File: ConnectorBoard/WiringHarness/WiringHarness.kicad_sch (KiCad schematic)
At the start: 36 parts, among them J1 Barrel_Jack, J3 Conn_ARM_SWD_TagConnect_TC203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, J4 Conn_02x05_Odd_Even, J5 Socket, J6 Qwiic, J7 Conn_02x12_Odd_Even, U1 PCA9306DCTR, U3 LDL212PV33R, U6 STM32C031G4Ux, U7 LDL212PU50R, U8 LD1085D2MTR

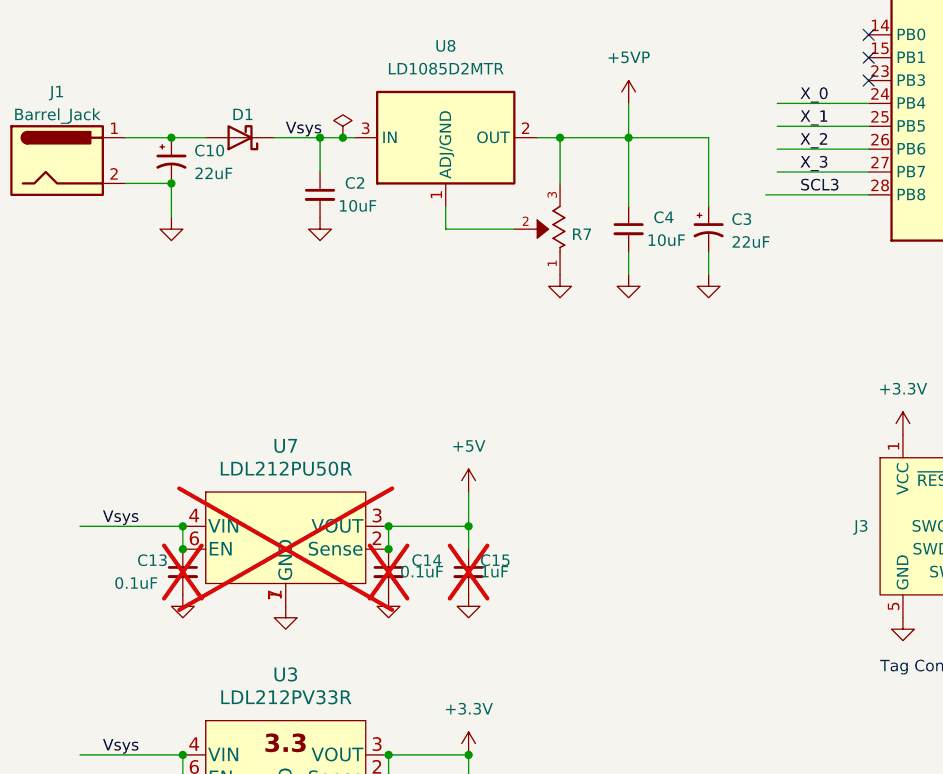
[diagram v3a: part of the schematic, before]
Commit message: switch to step models for many components
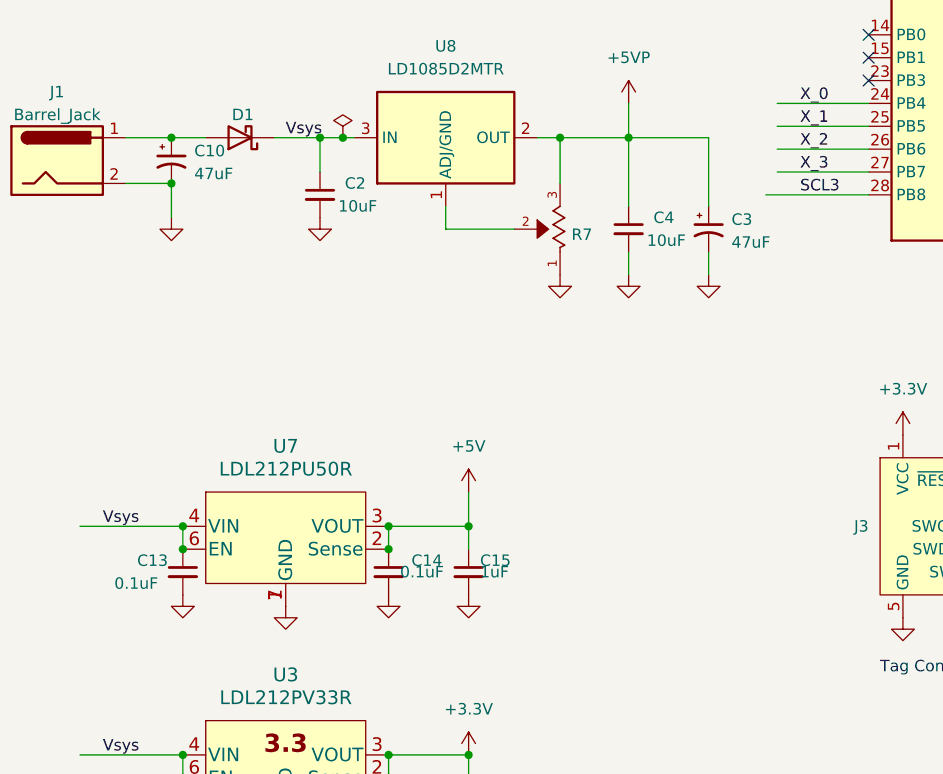
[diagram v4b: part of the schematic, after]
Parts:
- C10, C3: value 22uF -> 47uF; Digikey P16405CT-ND -> 10-ECE-A1EKA470ICT-ND; Vendor P16405CT-ND -> 10-ECE-A1EKA470ICT-ND
- C13, C14, C15, U7: now fitted
- C6: Vendor (none) -> CL10B105KA8NFNC; now left out of the parts list
- FB1: Vendor (none) -> 490-16660-1-ND; now left out of the parts list
- J6, U1: now left out of the parts list
- R1, R2: Digikey RMCF0603FT10K0DKR-ND -> RMCF0603FT10K0CT-ND; Vendor RMCF0603FT10K0DKR-ND -> RMCF0603FT10K0CT-ND; now left out of the parts list
- R7: Digikey TC33X-102ECT-ND -> TC33X-103ECT-ND; Vendor TC33X-102ECT-ND -> TC33X-103ECT-ND
- U6: Digikey 497-STM32C031G4U6-ND -> 497-STM32C031G6U6-ND; Vendor 497-STM32C031G4U6-ND -> 497-STM32C031G6U6-ND
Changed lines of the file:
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@@
       (effects (font (size 1.27 1.27)) hide)
     )
-    (property "Digikey" "497-STM32C031G4U6-ND" (at 129.54 52.07 0)
-      (effects (font (size 1.27 1.27)) hide)
-    )
-    (property "Vendor" "497-STM32C031G4U6-ND" (at 129.54 52.07 0)
+    (property "Digikey" "497-STM32C031G6U6-ND" (at 129.54 52.07 0)
+      (effects (font (size 1.27 1.27)) hide)
+    )
+    (property "Vendor" "497-STM32C031G6U6-ND" (at 129.54 52.07 0)
       (effects (font (size 1.27 1.27)) hide)
     )
@@
   )
   (symbol (lib_id "StockedComponents:C_1U") (at 198.12 60.96 0) (unit 1)
-    (in_bom yes) (on_board yes) (dnp yes) (fields_autoplaced)
+    (in_bom no) (on_board yes) (dnp yes) (fields_autoplaced)
     (property "Reference" "C6" (at 200.66 59.6963 0)
       (effects (font (size 1.27 1.27)) (justify left))
@@
     (property "Capacitance" "1uF" (at 200.66 62.2363 0)
       (effects (font (size 1.27 1.27)) (justify left))
+    )
+    (property "Vendor" "CL10B105KA8NFNC" (at 198.12 60.96 0)
+      (effects (font (size 1.27 1.27)) hide)
     )
     (pin "1")
@@
   )
   (symbol (lib_id "StockedComponents:PCA9306DQER") (at 189.23 120.65 0) (mirror y) (unit 1)
-    (in_bom yes) (on_board yes) (dnp yes)
+    (in_bom no) (on_board yes) (dnp yes)
     (property "Reference" "U1" (at 194.31 101.6 0)
       (effects (font (size 1.27 1.27)))
@@
       (effects (font (size 1.27 1.27)) (justify left))
     )
-    (property "Value" "22uF" (at 41.91 64.9732 0)
+    (property "Value" "47uF" (at 41.91 64.9732 0)
       (effects (font (size 1.27 1.27)) (justify left))
     )
@@
       (effects (font (size 1.27 1.27)) hide)
     )
-    (property "Vendor" "P16405CT-ND" (at 39.37 63.5 0)
-      (effects (font (size 1.27 1.27)) hide)
-    )
-    (property "Digikey" "P16405CT-ND" (at 39.37 63.5 0)
+    (property "Vendor" "10-ECE-A1EKA470ICT-ND" (at 39.37 63.5 0)
+      (effects (font (size 1.27 1.27)) hide)
+    )
+    (property "Digikey" "10-ECE-A1EKA470ICT-ND" (at 39.37 63.5 0)
       (effects (font (size 1.27 1.27)) hide)
     )
@@
       (effects (font (size 1.27 1.27)) (justify bottom) hide)
     )
-    (property "Digikey" "TC33X-102ECT-ND" (at 82.55 68.58 90)
-      (effects (font (size 1.27 1.27)) hide)
-    )
-    (property "Vendor" "TC33X-102ECT-ND" (at 82.55 68.58 0)
+    (property "Digikey" "TC33X-103ECT-ND" (at 82.55 68.58 90)
+      (effects (font (size 1.27 1.27)) hide)
+    )
+    (property "Vendor" "TC33X-103ECT-ND" (at 82.55 68.58 0)
       (effects (font (size 1.27 1.27)) hide)
     )
@@
       (effects (font (size 1.27 1.27)) (justify left))
     )
-    (property "Value" "22uF" (at 101.6 72.5932 0)
+    (property "Value" "47uF" (at 101.6 72.5932 0)
       (effects (font (size 1.27 1.27)) (justify left))
     )
@@
       (effects (font (size 1.27 1.27)) hide)
     )
-    (property "Vendor" "P16405CT-ND" (at 99.06 71.12 0)
-      (effects (font (size 1.27 1.27)) hide)
-    )
-    (property "Digikey" "P16405CT-ND" (at 99.06 71.12 0)
+    (property "Vendor" "10-ECE-A1EKA470ICT-ND" (at 99.06 71.12 0)
+      (effects (font (size 1.27 1.27)) hide)
+    )
+    (property "Digikey" "10-ECE-A1EKA470ICT-ND" (at 99.06 71.12 0)
       (effects (font (size 1.27 1.27)) hide)
     )
@@
   )
   (symbol (lib_id "Connector_Generic:Conn_01x04") (at 234.95 133.35 90) (mirror x) (unit 1)
-    (in_bom yes) (on_board yes) (dnp yes)
+    (in_bom no) (on_board yes) (dnp yes)
     (property "Reference" "J6" (at 236.22 137.16 90)
       (effects (font (size 1.27 1.27)))
@@
   )
   (symbol (lib_id "Device:R_Small_US") (at 240.03 107.95 0) (unit 1)
-    (in_bom yes) (on_board yes) (dnp yes) (fields_autoplaced)
+    (in_bom no) (on_board yes) (dnp yes) (fields_autoplaced)
     (property "Reference" "R1" (at 242.57 106.68 0)
       (effects (font (size 1.27 1.27)) (justify left) hide)
@@
       (effects (font (size 1.27 1.27)) hide)
     )
-    (property "Digikey" "RMCF0603FT10K0DKR-ND" (at 240.03 107.95 0)
-      (effects (font (size 1.27 1.27)) hide)
-    )
-    (property "Vendor" "RMCF0603FT10K0DKR-ND" (at 240.03 107.95 0)
+    (property "Digikey" "RMCF0603FT10K0CT-ND" (at 240.03 107.95 0)
+      (effects (font (size 1.27 1.27)) hide)
+    )
+    (property "Vendor" "RMCF0603FT10K0CT-ND" (at 240.03 107.95 0)
       (effects (font (size 1.27 1.27)) hide)
     )
@@
   )
   (symbol (lib_id "Device:C_Small") (at 72.39 109.22 0) (unit 1)
-    (in_bom yes) (on_board yes) (dnp yes)
+    (in_bom yes) (on_board yes) (dnp no)
     (property "Reference" "C15" (at 73.66 107.95 0)
       (effects (font (size 1.27 1.27)) (justify left))
@@
   )
   (symbol (lib_id "Device:R_Small_US") (at 237.49 107.95 0) (unit 1)
-    (in_bom yes) (on_board yes) (dnp yes) (fields_autoplaced)
+    (in_bom no) (on_board yes) (dnp yes) (fields_autoplaced)
     (property "Reference" "R2" (at 240.03 106.68 0)
       (effects (font (size 1.27 1.27)) (justify left) hide)
@@
       (effects (font (size 1.27 1.27)) hide)
     )
-    (property "Digikey" "RMCF0603FT10K0DKR-ND" (at 237.49 107.95 0)
-      (effects (font (size 1.27 1.27)) hide)
-    )
-    (property "Vendor" "RMCF0603FT10K0DKR-ND" (at 237.49 107.95 0)
+    (property "Digikey" "RMCF0603FT10K0CT-ND" (at 237.49 107.95 0)
+      (effects (font (size 1.27 1.27)) hide)
+    )
+    (property "Vendor" "RMCF0603FT10K0CT-ND" (at 237.49 107.95 0)
       (effects (font (size 1.27 1.27)) hide)
     )
@@
   )
   (symbol (lib_id "StockedComponents:FB_120_100MHz") (at 193.04 58.42 90) (unit 1)
-    (in_bom yes) (on_board yes) (dnp yes) (fields_autoplaced)
+    (in_bom no) (on_board yes) (dnp yes) (fields_autoplaced)
     (property "Reference" "FB1" (at 193.0019 54.61 90)
       (effects (font (size 1.27 1.27)))
@@
     )
     (property "DigiKey PN " "490-16660-1-ND" (at 200.66 59.69 0)
+      (effects (font (size 1.27 1.27)) hide)
+    )
+    (property "Vendor" "490-16660-1-ND" (at 193.04 58.42 0)
       (effects (font (size 1.27 1.27)) hide)
     )
@@
   )
   (symbol (lib_id "StockedComponents:LDL212PU50R") (at 35.56 105.41 0) (unit 1)
-    (in_bom yes) (on_board yes) (dnp yes) (fields_autoplaced)
+    (in_bom yes) (on_board yes) (dnp no) (fields_autoplaced)
     (property "Reference" "U7" (at 52.07 95.25 0)
       (effects (font (size 1.524 1.524)))
@@
   )
   (symbol (lib_id "Device:C_Small") (at 63.5 109.22 0) (unit 1)
-    (in_bom yes) (on_board yes) (dnp yes)
+    (in_bom yes) (on_board yes) (dnp no)
     (property "Reference" "C14" (at 66.04 107.95 0)
       (effects (font (size 1.27 1.27)) (justify left))
@@
   )
   (symbol (lib_id "Device:C_Small") (at 40.64 109.22 0) (unit 1)
-    (in_bom yes) (on_board yes) (dnp yes)
+    (in_bom yes) (on_board yes) (dnp no)
     (property "Reference" "C13" (at 35.56 107.95 0)
       (effects (font (size 1.27 1.27)) (justify left))

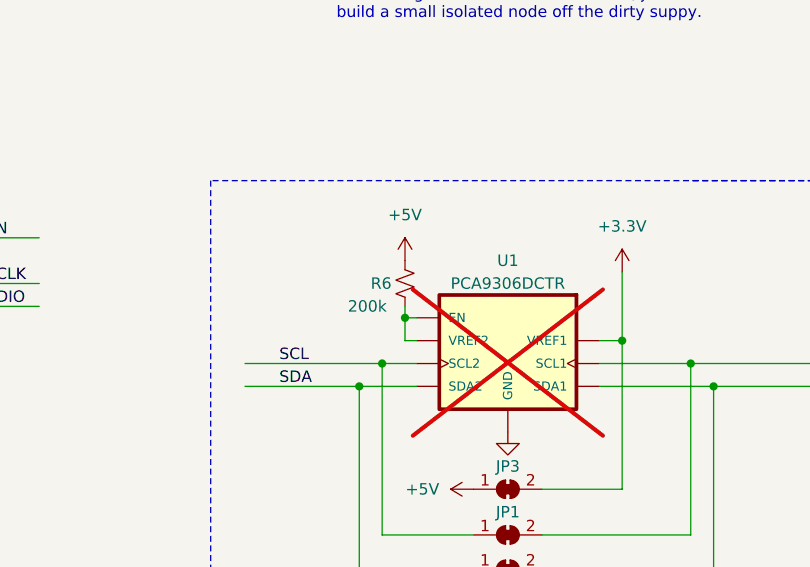
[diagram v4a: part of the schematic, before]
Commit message: add a DNP to the schematic.  Step/Dir works OK
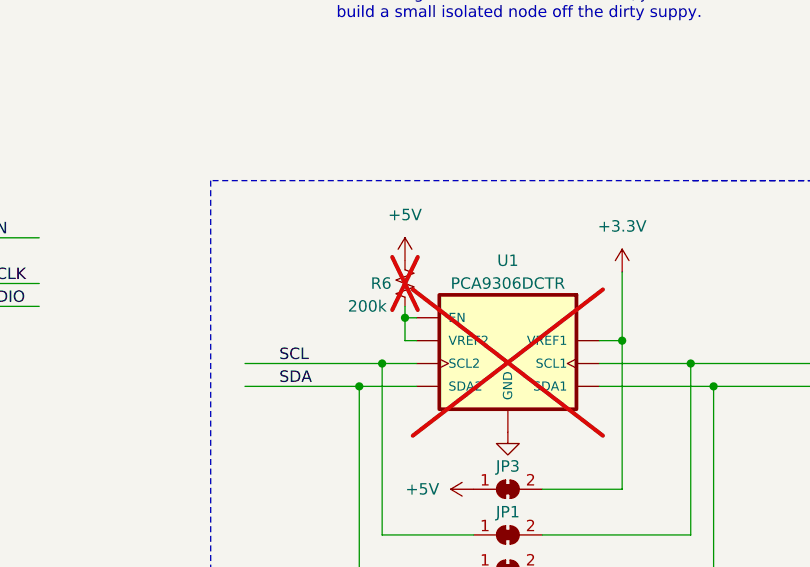
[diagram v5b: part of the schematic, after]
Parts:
- R6: now not fitted
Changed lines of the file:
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@@
   )
   (symbol (lib_id "Device:R_Small_US") (at 182.88 104.14 0) (unit 1)
-    (in_bom yes) (on_board yes) (dnp no)
+    (in_bom yes) (on_board yes) (dnp yes)
     (property "Reference" "R6" (at 179.07 104.14 0)
       (effects (font (size 1.27 1.27)) (justify left))
